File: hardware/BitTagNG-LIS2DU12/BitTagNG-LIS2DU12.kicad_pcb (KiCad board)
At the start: 2 copper layers, 16 x 9 mm, 22 parts, among them J201 CONN_02X04, J301 Conn_01x01, J302 Conn_01x01, J303 Conn_01x01, J304 Conn_01x01, J401 CONN_01X02, Q501 Q_NPN_BEC, U1 at25ex321D-UUN, U3 LIS2DW12TR, U302 stm32l431kc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

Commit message: updated latest board design
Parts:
- moved C502 0.92 mm to (144.8, 107.8)
- moved C3 0.76 mm to (143.2, 107.0), turned to 180 degrees
- moved Q501 0.73 mm to (145.0, 106.7), turned to -90 degrees
- moved C1 0.38 mm to (143.2, 107.8), turned to 180 degrees
- moved C2 0.17 mm to (143.2, 106.2)
- turned U3 to 90 degrees
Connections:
- U3 pad 3: /ACCEL_MISO -> unconnected-(U3-SDO/SA0-Pad3)
- U3 pad 4: /ACCEL_MOSI -> /ACCEL_SDI_SDO
- U3 pad 5: /WKUP4 -> GND
- U302 pad 10: /ACCEL_CS -> unconnected-(U302-PA4-Pad10)
- U302 pad 11: /ACCEL_SCK -> unconnected-(U302-PA5-Pad11)
- U302 pad 12: /ACCEL_MISO -> unconnected-(U302-PA6-Pad12)
- U302 pad 13: /ACCEL_MOSI -> unconnected-(U302-PA7-Pad13)
- U302 pad 6: unconnected-(U302-PA0-Pad6) -> /ACCEL_SDI_SDO
- U302 pad 7: unconnected-(U302-PA1-Pad7) -> /ACCEL_CS
- U302 pad 9: unconnected-(U302-PA3-Pad9) -> /ACCEL_SCK
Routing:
- net /ACCEL_MOSI: track 5.53 -> 0.00 mm, vias 1 -> 0
- net /ACCEL_MISO: track 4.78 -> 0.00 mm, vias 1 -> 0
- net VIN: track 40.0 -> 35.5 mm
- net /ACCEL_SDI_SDO: track 0.00 -> 1.87 mm, vias 0 -> 1
- net /ACCEL_SCK: track 2.55 -> 0.81 mm
- net Net-(Q501-C): track 7.41 -> 6.32 mm
- net GND: track 51.9 -> 51.2 mm, vias 6 -> 7

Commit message: working on compass board
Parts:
- U3: value LIS2DW12TR -> LIS2DU12TR; footprint AccelTag:LIS2DW12TR -> AccelTag:LGA-12L_LIS2DU12_STM
- moved U3 0.20 mm to (144.2, 109.7)
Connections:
- U3 pad 5: GND -> unconnected-(U3-NC-Pad5)

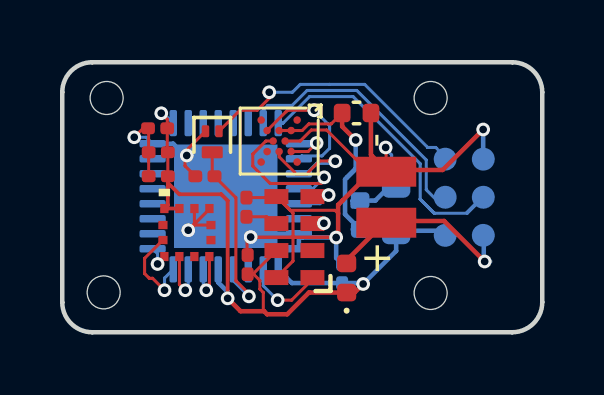
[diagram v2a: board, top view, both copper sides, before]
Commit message: designed compass tag
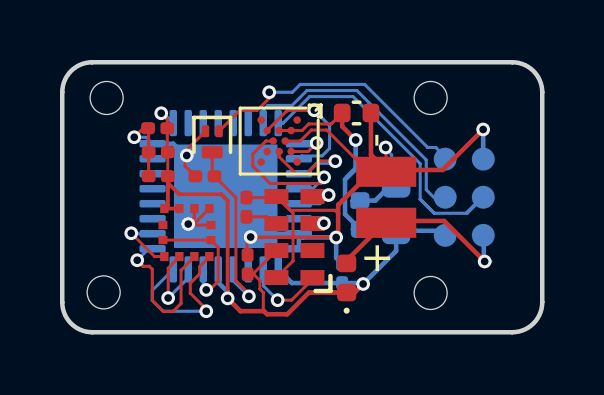
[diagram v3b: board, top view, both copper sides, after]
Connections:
- U3 pad 1: /ACCEL_SCK -> /USART2_CK
- U3 pad 12: /WKUP4 -> /WKUP1
- U3 pad 3: unconnected-(U3-SDO/SA0-Pad3) -> /USART2_RX
- U3 pad 4: /ACCEL_SDI_SDO -> /USART2_TX
- U3 pad 5: unconnected-(U3-NC-Pad5) -> /WKUP1
- U302 pad 10: unconnected-(U302-PA4-Pad10) -> /USART2_CK
- U302 pad 6: /ACCEL_SDI_SDO -> /WKUP1
- U302 pad 8: /WKUP4 -> /USART2_TX
- U302 pad 9: /ACCEL_SCK -> /USART2_RX
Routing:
- net /USART2_TX: track 0.00 -> 5.70 mm, vias 0 -> 1
- net /USART2_RX: track 0.00 -> 5.30 mm, vias 0 -> 1
- net /WKUP1: track 0.00 -> 4.32 mm, vias 0 -> 1
- net /WKUP4: track 3.23 -> 0.00 mm, vias 1 -> 0
- net /USART2_CK: track 0.00 -> 2.25 mm, vias 0 -> 1
- net /ACCEL_SDI_SDO: track 2.04 -> 0.00 mm, vias 1 -> 0
- net /ACCEL_SCK: track 0.92 -> 0.00 mm, vias 1 -> 0
- net /ACCEL_CS: track 1.97 -> 2.80 mm
